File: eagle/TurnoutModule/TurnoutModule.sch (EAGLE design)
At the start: 15 parts, among them IC1 L293D, IC2 MCP23008/P

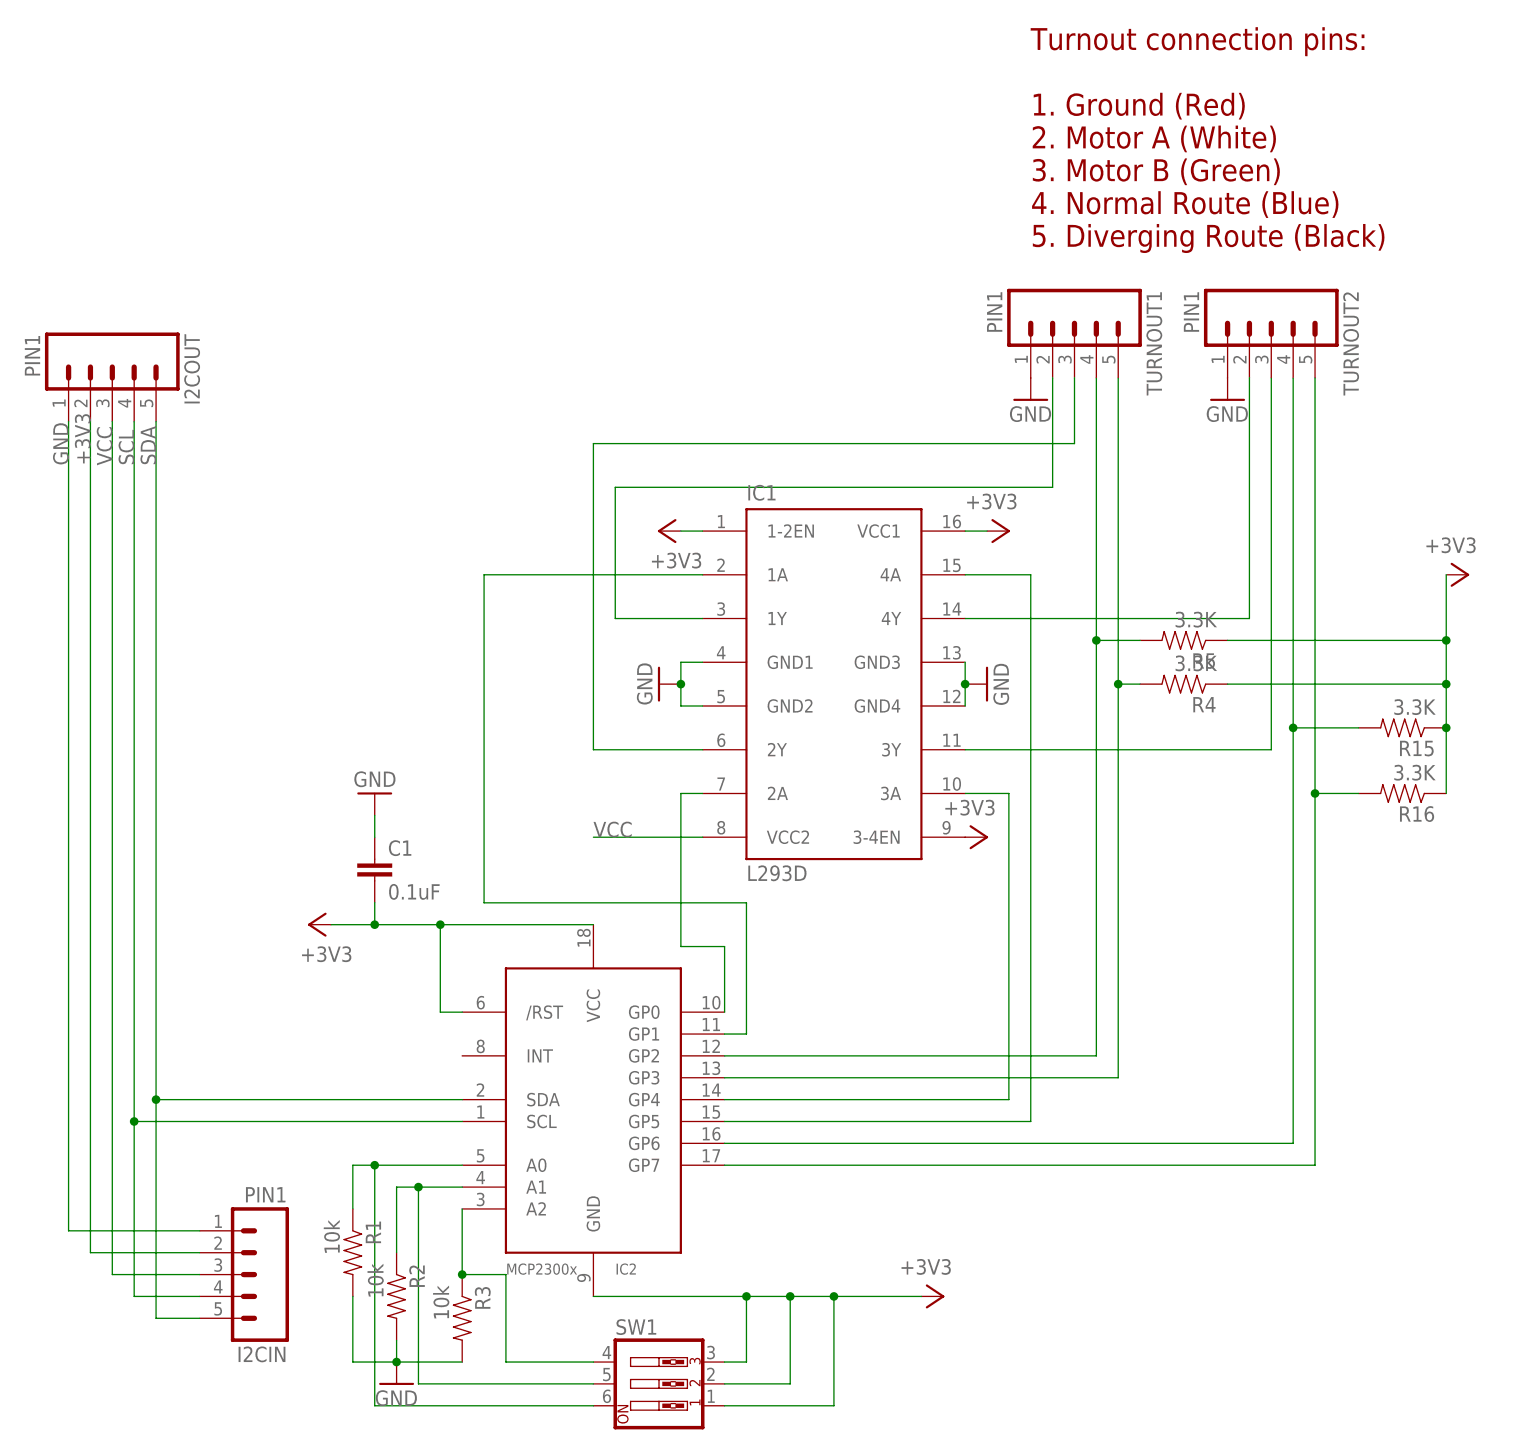
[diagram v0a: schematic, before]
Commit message: 1.  Cleanup continues.  BlockController and the corresponding controller are deprecated along with SignalController and it's controller board.  These are replaced by the InputModule and OutputModule respectively 2.  TurnoutHandler moved to the MultiModuleController project folder 3.  Module moved to the MultiModuleController project folder 4.  More database cleanup work completed.
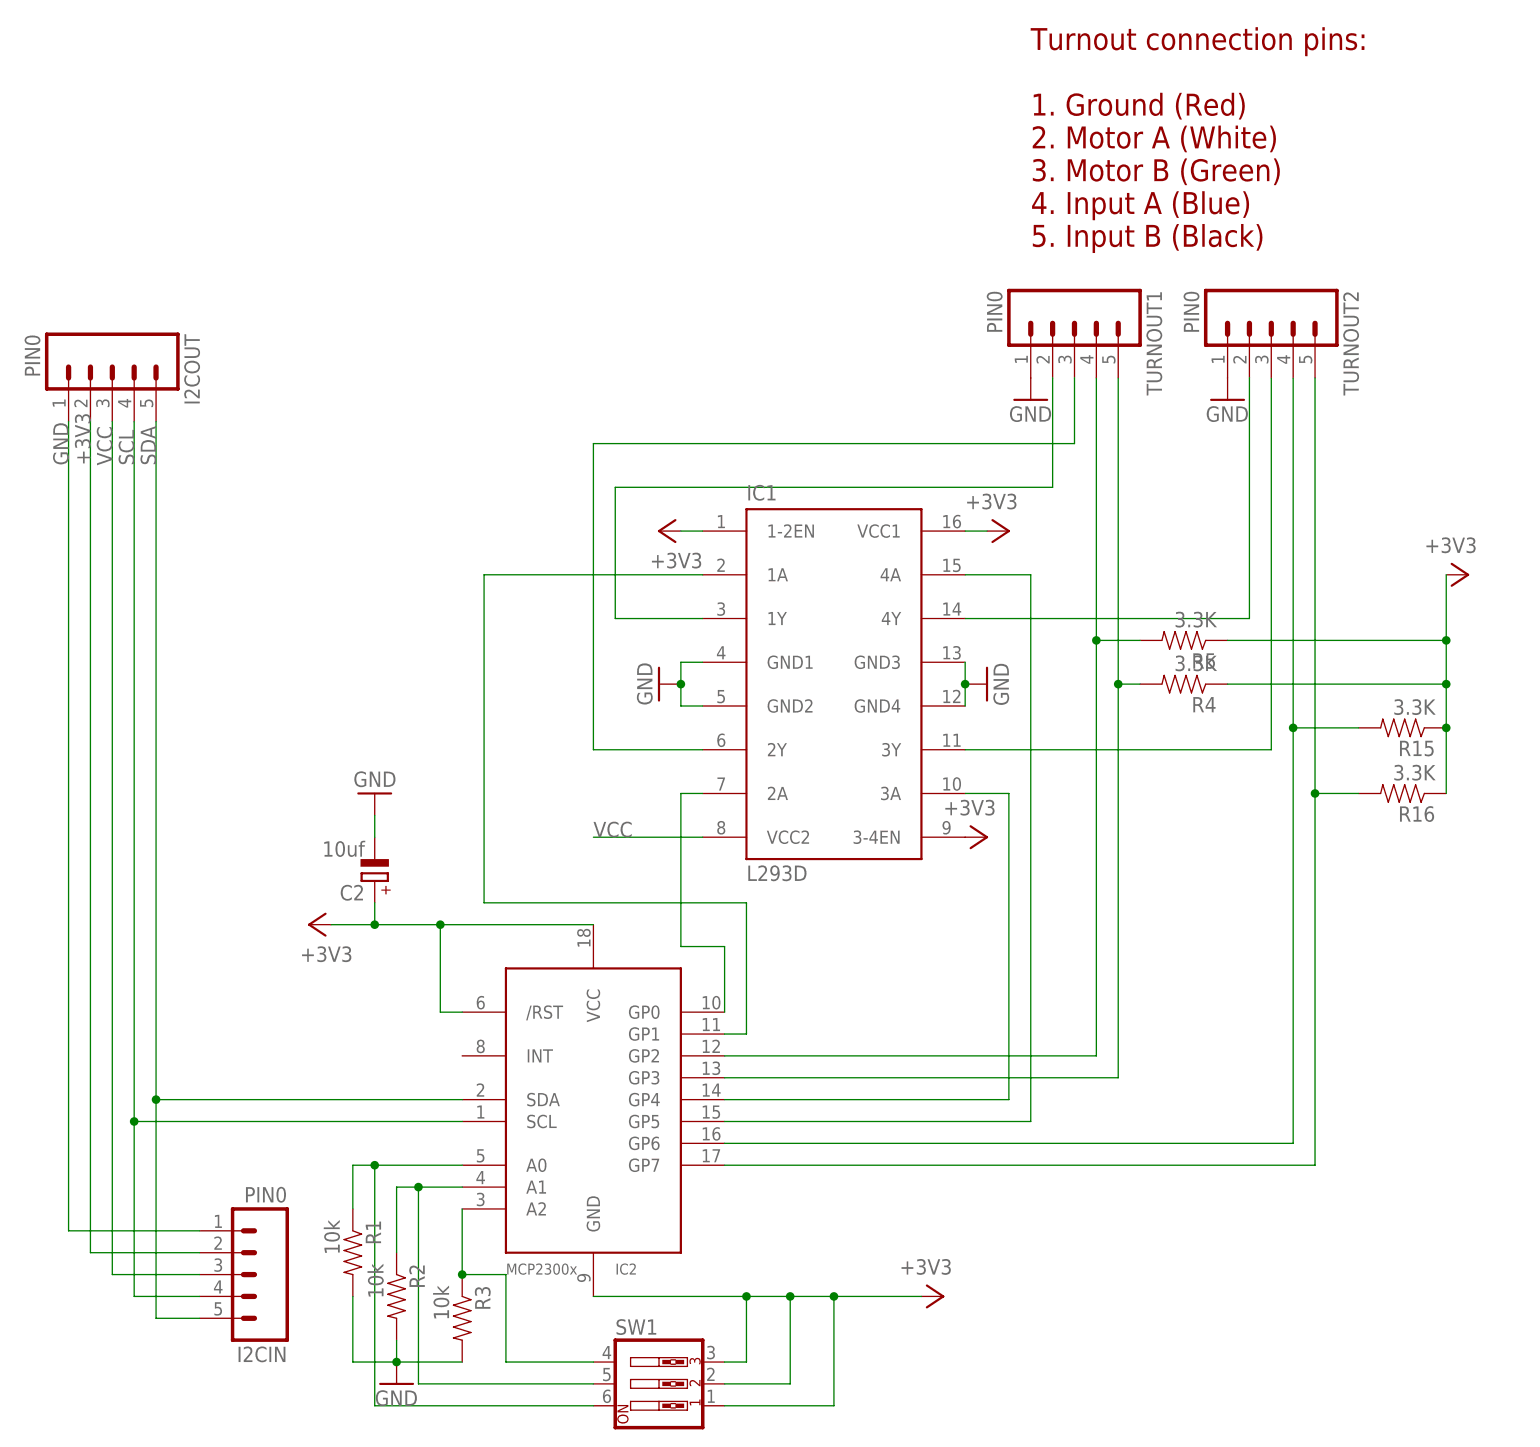
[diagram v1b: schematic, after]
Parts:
- removed C1: 0.1uF, SparkFun-Capacitors:CAPPTH
- added C2: 10uf, rcl:CPOL-EUE2.5-6
- I2CIN, I2COUT, TURNOUT1, TURNOUT2: value PIN1 -> PIN0
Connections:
- net +3V3: now also C2.+; no longer C1.2
- net GND: now also C2.-; no longer C1.1
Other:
- note added: "Turnout connection pins: 1. Ground (Red) 2. Motor A (White) 3. Motor B (Green) 4. Input A (Blue) 5. Input B (Black)"
- note removed: "Turnout connection pins: 1. Ground (Red) 2. Motor A (White) 3. Motor B (Green) 4. Normal Route (Blue) 5. Diverging Route (Black)"
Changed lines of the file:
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@@
 </classes>
 <parts>
-<part name="TURNOUT1" library="con-amp-quick" deviceset="M05" device="" value="PIN1"/>
+<part name="TURNOUT1" library="con-amp-quick" deviceset="M05" device="" value="PIN0"/>
 <part name="GND6" library="SparkFun-Aesthetics" deviceset="GND" device=""/>
 <part name="R15" library="SparkFun-Resistors" deviceset="RESISTOR" device="PTH-1/4W" value="3.3K"/>
 <part name="R16" library="SparkFun-Resistors" deviceset="RESISTOR" device="PTH-1/4W" value="3.3K"/>
-<part name="TURNOUT2" library="con-amp-quick" deviceset="M05" device="" value="PIN1"/>
+<part name="TURNOUT2" library="con-amp-quick" deviceset="M05" device="" value="PIN0"/>
 <part name="IC1" library="st-microelectronics" deviceset="L293D" device=""/>
 <part name="GND12" library="SparkFun-Aesthetics" deviceset="GND" device=""/>
@@
 <part name="+3V6" library="supply1" deviceset="+3V3" device=""/>
 <part name="IC2" library="adafruit" deviceset="MCP23008" device="/P"/>
-<part name="I2COUT" library="con-amp-quick" deviceset="M05" device="" value="PIN1"/>
-<part name="I2CIN" library="con-amp-quick" deviceset="M05" device="" value="PIN1"/>
-<part name="C1" library="SparkFun-Capacitors" deviceset="CAP" device="PTH" value="0.1uF"/>
+<part name="I2COUT" library="con-amp-quick" deviceset="M05" device="" value="PIN0"/>
+<part name="I2CIN" library="con-amp-quick" deviceset="M05" device="" value="PIN0"/>
 <part name="GND1" library="SparkFun-Aesthetics" deviceset="GND" device=""/>
 <part name="R1" library="SparkFun-Resistors" deviceset="RESISTOR" device="PTH-1/4W" value="10k"/>
@@
 <part name="+3V1" library="supply1" deviceset="+3V3" device=""/>
 <part name="GND3" library="SparkFun-Aesthetics" deviceset="GND" device=""/>
+<part name="C2" library="rcl" deviceset="CPOL-EU" device="E2.5-6" value="10uf"/>
 </parts>
 <sheets>
@@
 2. Motor A (White)
 3. Motor B (Green)
-4. Normal Route (Blue)
-5. Diverging Route (Black)</text>
+4. Input A (Blue)
+5. Input B (Black)</text>
 </plain>
 <instances>
@@
 <instance part="I2COUT" gate="G$1" x="-2.54" y="142.24" rot="R270"/>
 <instance part="I2CIN" gate="G$1" x="15.24" y="35.56" rot="R180"/>
-<instance part="C1" gate="G$1" x="27.94" y="81.28"/>
 <instance part="GND1" gate="1" x="27.94" y="91.44" rot="R180"/>
 <instance part="R1" gate="G$1" x="25.4" y="38.1" rot="R270"/>
@@
 <instance part="+3V1" gate="G$1" x="93.98" y="33.02" rot="R270"/>
 <instance part="GND3" gate="1" x="30.48" y="22.86"/>
+<instance part="C2" gate="G$1" x="27.94" y="81.28" rot="R180"/>
 </instances>
 <busses>
@@
 </segment>
 <segment>
-<pinref part="C1" gate="G$1" pin="1"/>
 <pinref part="GND1" gate="1" pin="GND"/>
 <wire x1="27.94" y1="88.9" x2="27.94" y2="86.36" width="0.1524" layer="91"/>
+<pinref part="C2" gate="G$1" pin="-"/>
 </segment>
 <segment>
@@
 <wire x1="35.56" y1="66.04" x2="35.56" y2="76.2" width="0.1524" layer="91"/>
 <junction x="35.56" y="76.2"/>
-<pinref part="C1" gate="G$1" pin="2"/>
 <wire x1="27.94" y1="76.2" x2="27.94" y2="78.74" width="0.1524" layer="91"/>
 <junction x="27.94" y="76.2"/>
-</segment>
-<segment>
+<pinref part="C2" gate="G$1" pin="+"/>
+</segment>
+<segment>
